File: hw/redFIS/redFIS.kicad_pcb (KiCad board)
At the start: 2 copper layers, 72 parts, among them J1 USB_B, J2 DE9_Plug, J3 Conn_01x04, J4 Conn_01x03, Q1 BC850, Q2 BC850, Q3 BC850, Q4 BC857, U1 ESP-32S, U2 AP63203WU, U3 AP63205WU, U4 TJA1049T, U5 CH340G, U6 PCM5102A, U7 AP63203WU, Y1 12Mhz

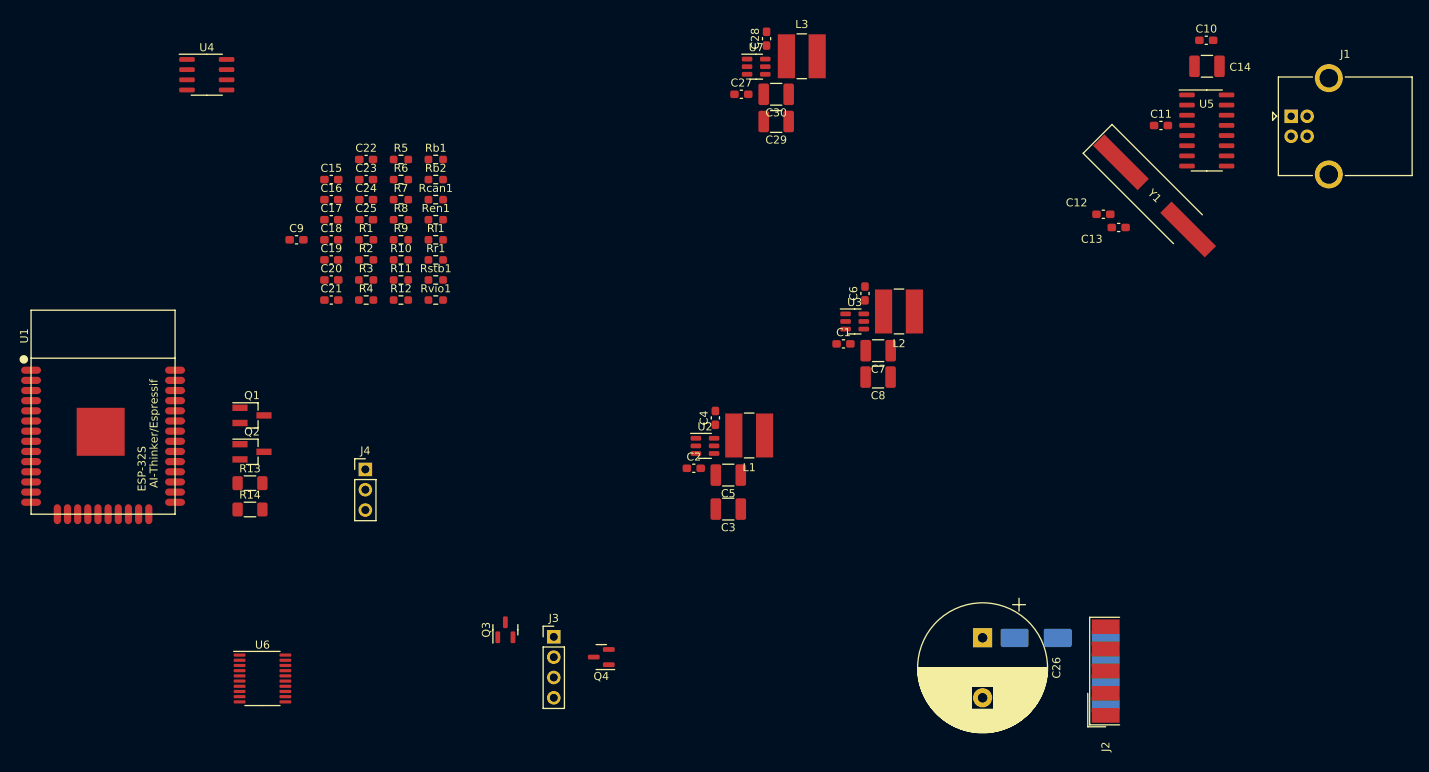
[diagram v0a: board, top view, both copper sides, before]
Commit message: Finished first version of PCB
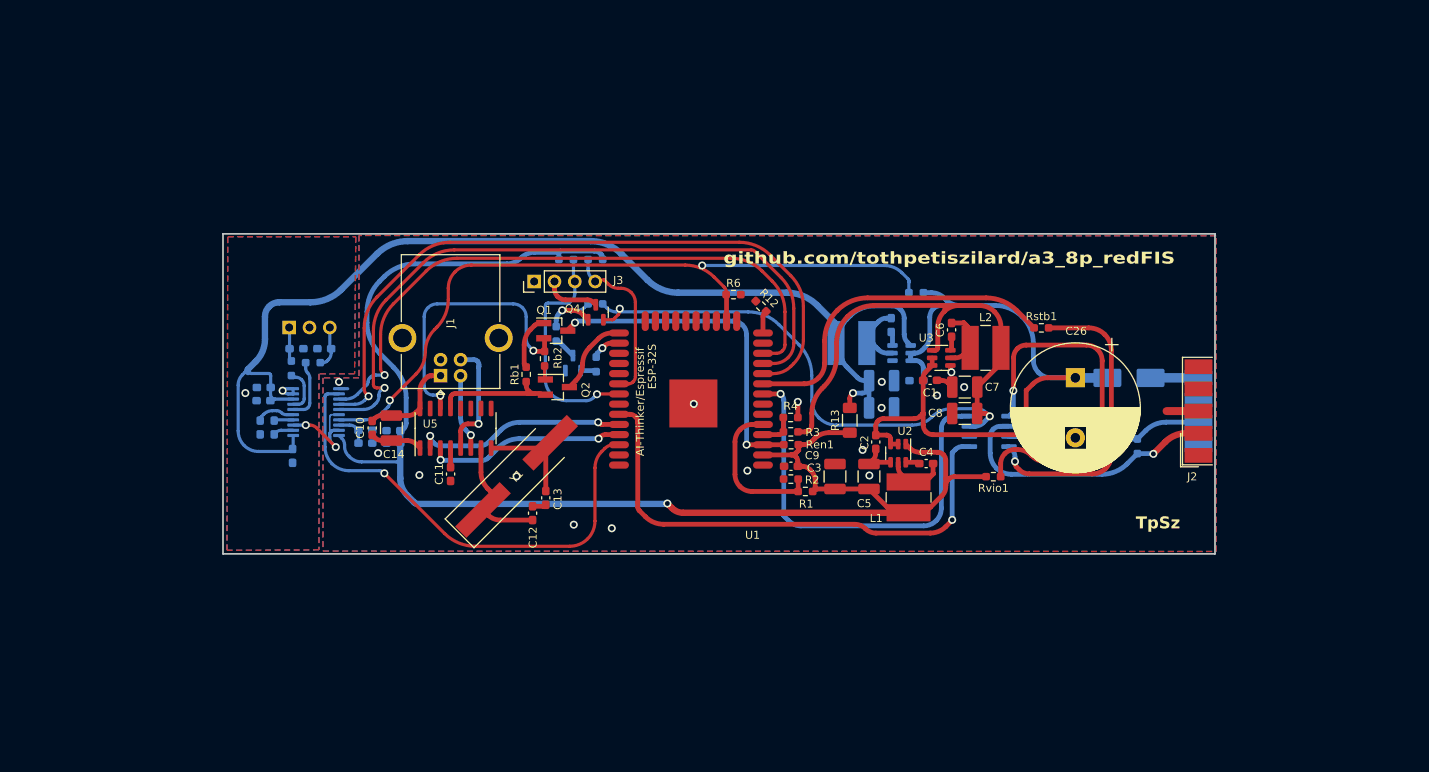
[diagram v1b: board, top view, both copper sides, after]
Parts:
- removed R14: 1R, Resistor_SMD:R_1206_3216Metric_Pad1.30x1.75mm_HandSolder
- C15, C16, C17, C18, C19, C20, C21, C22, C23, C24, C25, C27, C28, C29, C30, J4, L3, Q3, R10, R11, R5, R7, R8, R9, Rcan1, Rl1, Rr1, U4, U6, U7: moved to B.Cu
- moved C10 115.0 mm to (68.7, 74.2), turned to 90 degrees
- moved C14 111.5 mm to (71.0, 74.3), turned to -90 degrees
- moved J1 111.2 mm to (77.2, 67.7), turned to 90 degrees
- moved U4 107.5 mm to (145.8, 74.7)
- moved U5 101.0 mm to (79.1, 74.3), turned to 90 degrees
- moved C11 98.9 mm to (78.5, 80.0), turned to 90 degrees
- moved Rcan1 93.0 mm to (164.3, 76.5), turned to 90 degrees
- moved Y1 87.1 mm to (86.7, 80.3), turned to 45 degrees
- moved C12 80.5 mm to (88.7, 84.9), turned to -90 degrees
- moved C13 79.2 mm to (90.3, 83.0), turned to 90 degrees
- moved Rstb1 75.9 mm to (152.3, 61.8)
- moved R13 75.4 mm to (128.3, 73.3), turned to 90 degrees
- moved U1 73.7 mm to (108.4, 69.4), turned to 180 degrees
- moved Rvio1 73.1 mm to (146.3, 80.3), turned to 180 degrees
- moved C9 68.0 mm to (121.0, 79.0), turned to 180 degrees
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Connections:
- U1 pad 16: unconnected-(U1-IO13-Pad16) -> MUTE
- U1 pad 7: MUTE -> unconnected-(U1-IO35-Pad7)
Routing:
- net +3V3: track 0.00 -> 190.1 mm, vias 0 -> 1
- net +3.3VA: track 0.00 -> 147.2 mm, vias 0 -> 1
- net +5V: track 0.00 -> 124.6 mm, vias 0 -> 2
- net MUTE: track 0.00 -> 93.3 mm, vias 0 -> 2
- net +12V: track 0.00 -> 90.8 mm
- net I2S_DOUT: track 0.00 -> 88.7 mm, vias 0 -> 1
- net I2S_LRC: track 0.00 -> 86.8 mm, vias 0 -> 1
- net I2S_BCLK: track 0.00 -> 78.6 mm, vias 0 -> 1
- net CANTXD: track 0.00 -> 65.3 mm, vias 0 -> 1
- net I2S_SCK: track 0.00 -> 60.4 mm, vias 0 -> 1
- net CANRXD: track 0.00 -> 53.3 mm, vias 0 -> 1
- net Net-(U4-SPLIT): track 0.00 -> 48.2 mm, vias 0 -> 1
- net STB: track 0.00 -> 42.4 mm
- net ESP_EN: track 0.00 -> 42.1 mm, vias 0 -> 2
- net GND: track 0.00 -> 39.7 mm, vias 0 -> 20
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- added copper zone on B.Cu, net GND
- added copper zone on F.Cu, net GND
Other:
- board outline added: 124 x 40 mm
- board text added: "Audi A3 8P Red FIS Project v1.0"
- board text added: "L G R"
- board text added: "TpSz"
- board text added: "github.com/tothpetiszilard/a3_8p_redFIS"

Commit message: HW design bugfix
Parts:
- added Q5: BC850, Package_TO_SOT_SMD:SOT-23, B.Cu at (156.6, 85.1)
- added Q6: BC857, Package_TO_SOT_SMD:SOT-23, B.Cu at (143.7, 82.5)
- added R14: 10k, Resistor_SMD:R_0603_1608Metric_Pad0.98x0.95mm_HandSolder, B.Cu at (131.4, 85.5)
- added R15: 5k, Resistor_SMD:R_0603_1608Metric_Pad0.98x0.95mm_HandSolder, B.Cu at (135.2, 86.5)
- added R16: 10k, Resistor_SMD:R_0603_1608Metric_Pad0.98x0.95mm_HandSolder, B.Cu at (149.3, 84.8)
- added R17: 10k, Resistor_SMD:R_0603_1608Metric_Pad0.98x0.95mm_HandSolder, B.Cu at (143.7, 85.7)
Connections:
- U4 pad 1: CANTXD -> Net-(Q6-C)
- U4 pad 4: CANRXD -> Net-(U4-RXD)
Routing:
- net CANRXD: track 53.3 -> 32.2 mm
- net Net-(U4-RXD): track 0.00 -> 19.3 mm

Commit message: Finished bugfixing of HW design v1
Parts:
- moved Q5 10.1 mm to (146.8, 82.6), turned to 0 degrees
- moved R16 7.34 mm to (142.3, 82.6)
- moved Q6 3.22 mm to (142.4, 79.5)
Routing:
- net +5V: track 124.6 -> 136.7 mm
- net CANTXD: track 65.3 -> 56.1 mm
- net Net-(Q5-C): track 0.00 -> 6.69 mm
- net Net-(Q6-C): track 0.00 -> 3.27 mm
- net Net-(Q5-B): track 0.00 -> 3.00 mm
- net Net-(U4-RXD): track 19.3 -> 18.4 mm
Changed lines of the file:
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@@
 	(footprint "Package_TO_SOT_SMD:SOT-23"
 		(layer "B.Cu")
-		(at 156.6 85.0625 90)
+		(at 146.8 82.6)
 		(descr "SOT, 3 Pin (https://www.jedec.org/system/files/docs/to-236h.pdf variant AB), generated with kicad-footprint-generator ipc_gullwing_generator.py")
 		(tags "SOT TO_SOT_SMD")
 		(property "Reference" "Q5"
-			(at 0 2.4 90)
+			(at 0 2.4 360)
 			(layer "B.SilkS")
 			(effects
@@
 		)
 		(property "Value" "BC850"
-			(at 0 -2.4 90)
+			(at 0 -2.4 360)
 			(layer "B.Fab")
 			(effects
@@
 		)
 		(property "Footprint" "Package_TO_SOT_SMD:SOT-23"
-			(at 0 0 90)
+			(at 0 0 360)
 			(layer "B.Fab")
 			(hide yes)
@@
 		)
 		(property "Datasheet" "http://www.infineon.com/dgdl/Infineon-BC847SERIES_BC848SERIES_BC849SERIES_BC850SERIES-DS-v01_01-en.pdf?fileId=db3a304314dca389011541d4630a1657"
-			(at 0 0 90)
+			(at 0 0 360)
 			(layer "B.Fab")
 			(hide yes)
@@
 		)
 		(property "Description" "0.1A Ic, 45V Vce, NPN Transistor, SOT-23"
-			(at 0 0 90)
+			(at 0 0 360)
 			(layer "B.Fab")
 			(hide yes)
@@
 		(attr smd)
 		(fp_line
-			(start 0.65 -1.56)
-			(end 0 -1.56)
+			(start -1.675 1.56)
+			(end 0 1.56)
 			(stroke
 				(width 0.12)
@@
 		)
 		(fp_line
-			(start 0.65 1.56)
-			(end 0 1.56)
+			(start 0.65 -1.56)
+			(end 0 -1.56)
 			(stroke
 				(width 0.12)
@@
 		)
 		(fp_line
-			(start -1.675 1.56)
+			(start 0.65 1.56)
 			(end 0 1.56)
 			(stroke
@@
 		)
 		(fp_line
-			(start 1.92 -1.7)
-			(end -1.92 -1.7)
+			(start -1.92 -1.7)
+			(end -1.92 1.7)
 			(stroke
 				(width 0.05)
@@
 		)
 		(fp_line
-			(start -1.92 -1.7)
-			(end -1.92 1.7)
+			(start -1.92 1.7)
+			(end 1.92 1.7)
 			(stroke
 				(width 0.05)
@@
 		)
 		(fp_line
-			(start 1.92 1.7)
-			(end 1.92 -1.7)
+			(start 1.92 -1.7)
+			(end -1.92 -1.7)
 			(stroke
 				(width 0.05)
@@
 		)
 		(fp_line
-			(start -1.92 1.7)
-			(end 1.92 1.7)
+			(start 1.92 1.7)
+			(end 1.92 -1.7)
 			(stroke
 				(width 0.05)
@@
 		)
 		(fp_line
-			(start 0.65 -1.45)
-			(end 0.65 1.45)
+			(start -0.65 -1.45)
+			(end 0.65 -1.45)
 			(stroke
 				(width 0.1)
@@
 		)
 		(fp_line
-			(start -0.65 -1.45)
-			(end 0.65 -1.45)
+			(start -0.65 1.125)
+			(end -0.65 -1.45)
 			(stroke
 				(width 0.1)
@@
 		)
 		(fp_line
-			(start -0.65 1.125)
-			(end -0.65 -1.45)
+			(start -0.325 1.45)
+			(end -0.65 1.125)
 			(stroke
 				(width 0.1)
@@
 		)
 		(fp_line
-			(start 0.65 1.45)
-			(end -0.325 1.45)
+			(start 0.65 -1.45)
+			(end 0.65 1.45)
 			(stroke
 				(width 0.1)
@@
 		)
 		(fp_line
-			(start -0.325 1.45)
-			(end -0.65 1.125)
+			(start 0.65 1.45)
+			(end -0.325 1.45)
 			(stroke
 				(width 0.1)
@@
 		)
 		(fp_text user "${REFERENCE}"
-			(at 0 0 90)
+			(at 0 0 360)
 			(layer "B.Fab")
 			(effects
@@
 		)
 		(pad "1" smd roundrect
-			(at -0.9375 0.95 90)
+			(at -0.9375 0.95)
 			(size 1.475 0.6)
 			(layers "B.Cu" "B.Paste" "B.Mask")
@@
 		)
 		(pad "2" smd roundrect
-			(at -0.9375 -0.95 90)
+			(at -0.9375 -0.95)
 			(size 1.475 0.6)
 			(layers "B.Cu" "B.Paste" "B.Mask")
@@
 		)
 		(pad "3" smd roundrect
-			(at 0.9375 0 90)
+			(at 0.9375 0)
 			(size 1.475 0.6)
 			(layers "B.Cu" "B.Paste" "B.Mask")
@@
 	(footprint "Package_TO_SOT_SMD:SOT-23"
 		(layer "B.Cu")
-		(at 143.7 82.4875 90)
+		(at 142.4 79.5375 90)
 		(descr "SOT, 3 Pin (https://www.jedec.org/system/files/docs/to-236h.pdf variant AB), generated with kicad-footprint-generator ipc_gullwing_generator.py")
 		(tags "SOT TO_SOT_SMD")
@@
 	(footprint "Resistor_SMD:R_0603_1608Metric_Pad0.98x0.95mm_HandSolder"
 		(layer "B.Cu")
-		(at 149.3125 84.8)
+		(at 142.3125 82.6)
 		(descr "Resistor SMD 0603 (1608 Metric), square (rectangular) end terminal, IPC_7351 nominal with elongated pad for handsoldering. (Body size source: IPC-SM-782 page 72, https://www.pcb-3d.com/wordpress/wp-content/uploads/ipc-sm-782a_amendment_1_and_2.pdf), generated with kicad-footprint-generator")
 		(tags "resistor handsolder")
@@
 	)
 	(segment
+		(start 140.4 80.2)
+		(end 140.675 80.475)
+		(width 0.4)
+		(layer "B.Cu")
+		(net 8)
+	)
+	(segment
+		(start 140.4 74.4)
+		(end 140.4 80.2)
+		(width 0.4)
+		(layer "B.Cu")
+		(net 8)
+	)
+	(segment
 		(start 119.493792 61.343792)
 		(end 122.006207 63.856207)
@@
 	)
 	(segment
+		(start 140.75 74.05)
+		(end 140.4 74.4)
+		(width 0.4)
+		(layer "B.Cu")
+		(net 8)
+	)
+	(segment
+		(start 141.4 82.6)
+		(end 141.4 80.525)
+		(width 0.4)
+		(layer "B.Cu")
+		(net 8)
+	)
+	(segment
 		(start 145.85 72.8)
 		(end 145.375 72.325)
@@
 	)
 	(segment
+		(start 140.675 80.475)
+		(end 141.45 80.475)
+		(width 0.4)
+		(layer "B.Cu")
+		(net 8)
+	)
+	(segment
 		(start 97.9625 59.25)
 		(end 97.4625 58.75)
@@
 	)
 	(segment
+		(start 141.4 80.525)
+		(end 141.45 80.475)
+		(width 0.4)
+		(layer "B.Cu")
+		(net 8)
+	)
+	(segment
+		(start 143.3 74.05)
+		(end 140.75 74.05)
+		(width 0.4)
+		(layer "B.Cu")
+		(net 8)
+	)
+	(segment
 		(start 143.95 74.05)
 		(end 143.3 74.05)
@@
 	)
 	(segment
-		(start 141.15 85.75)
-		(end 141.15 77.385355)
-		(width 0.6)
-		(layer "B.Cu")
-		(net 60)
-	)
-	(segment
-		(start 141.225 77.275)
-		(end 141.175 77.325)
-		(width 0.6)
-		(layer "B.Cu")
-		(net 60)
-	)
-	(segment
-		(start 141.225 77.275)
-		(end 141.555 76.945)
-		(width 0.6)
-		(layer "B.Cu")
-		(net 60)
-	)
-	(segment
-		(start 142.412045 76.59)
-		(end 143.3 76.59)
+		(start 142.6875 85.75)
+		(end 142.7375 85.7)
 		(width 0.6)
 		(layer "B.Cu")
@@
 		(net 60)
 	)
-	(arc
-		(start 142.412045 76.59)
-		(mid 141.948215 76.682261)
-		(end 141.555 76.945)
-		(width 0.6)
-		(layer "B.Cu")
-		(net 60)
-	)
-	(arc
-		(start 141.175 77.325)
-		(mid 141.156497 77.352691)
-		(end 141.15 77.385355)
+	(segment
+		(start 141.15 85.75)
+		(end 142.6875 85.75)
 		(width 0.6)
 		(layer "B.Cu")
@@
 	)
 	(segment
-		(start 142.290858 72.8)
-		(end 141.336396 72.8)
-		(width 0.6)
+		(start 145.1 85.7)
+		(end 145.8625 84.9375)
+		(width 0.4)
 		(layer "B.Cu")
-		(net 85)
+		(net 82)
 	)
 	(segment
-		(start 137.580761 86.5)
-		(end 136.0625 86.5)
-		(width 0.6)
+		(start 145.8625 84.9375)
+		(end 145.8625 83.55)
+		(width 0.4)
 		(layer "B.Cu")
-		(net 85)
+		(net 82)
+	)
+	(segment
+		(start 144.5625 85.7)
+		(end 145.1 85.7)
+		(width 0.4)
+		(layer "B.Cu")
+		(net 82)
+	)
+	(segment
+		(start 143.225 80.6)
+		(end 143.35 80.475)
+		(width 0.4)
+		(layer "B.Cu")
+		(net 83)
+	)
+	(segment
+		(start 143.225 82.6)
+		(end 147.7375 82.6)
+		(width 0.4)
+		(layer "B.Cu")
+		(net 83)
 	)
 	(segment
-		(start 139.8 74.336396)
-		(end 139.8 84.280761)
+		(start 143.225 82.6)
+		(end 143.225 80.6)
+		(width 0.4)
+		(layer "B.Cu")
+		(net 83)
+	)
+	(segment
+		(start 142.412045 76.59)
+		(end 143.3 76.59)
 		(width 0.6)
 		(layer "B.Cu")
-		(net 85)
+		(net 84)
 	)
 	(segment
-		(start 142.339143 72.78)
-		(end 143.3 72.78)
+		(start 142.4 78.6)
+		(end 142.4 77.49)
+		(width 0.4)
+		(layer "B.Cu")
+		(net 84)
+	)
+	(segment
+		(start 142.4 77.49)
+		(end 143.3 76.59)
+		(width 0.4)
+		(layer "B.Cu")
+		(net 84)
+	)
+	(segment
+		(start 143.3 72.78)
+		(end 142.339143 72.78)
 		(width 0.6)
 		(layer "B.Cu")
 		(net 85)
 	)
-	(arc
-		(start 140.25 73.25)
-		(mid 139.916951 73.748442)
-		(end 139.8 74.336396)
+	(segment
+		(start 139 83.5625)
+		(end 136.0625 86.5)
 		(width 0.6)
 		(layer "B.Cu")
 		(net 85)
 	)
-	(arc
-		(start 142.315001 72.79)
-		(mid 142.303924 72.797401)
-		(end 142.290858 72.8)
+	(segment
+		(start 139 74.2)
+		(end 139 83.5625)
 		(width 0.6)
 		(layer "B.Cu")
 		(net 85)
 	)
-	(arc
-		(start 142.339143 72.78)
-		(mid 142.326077 72.782598)
-		(end 142.315001 72.79)
+	(segment
+		(start 142.290858 72.8)
+		(end 140.4 72.8)
 		(width 0.6)
 		(layer "B.Cu")
 		(net 85)
 	)
-	(arc
-		(start 139.15 85.85)
-		(mid 138.430027 86.33107)
-		(end 137.580761 86.5)
+	(segment
+		(start 140.4 72.8)
+		(end 139 74.2)
 		(width 0.6)
 		(layer "B.Cu")
@@
 	)
 	(arc
-		(start 141.336396 72.8)
-		(mid 140.748442 72.916951)
-		(end 140.25 73.25)
+		(start 142.339143 72.78)
+		(mid 142.326077 72.782598)
+		(end 142.315001 72.79)
 		(width 0.6)
 		(layer "B.Cu")
@@
 	)
 	(arc
-		(start 139.8 84.280761)
-		(mid 139.63107 85.130027)
-		(end 139.15 85.85)
+		(start 142.315001 72.79)
+		(mid 142.303924 72.797401)
+		(end 142.290858 72.8)
 		(width 0.6)
 		(layer "B.Cu")

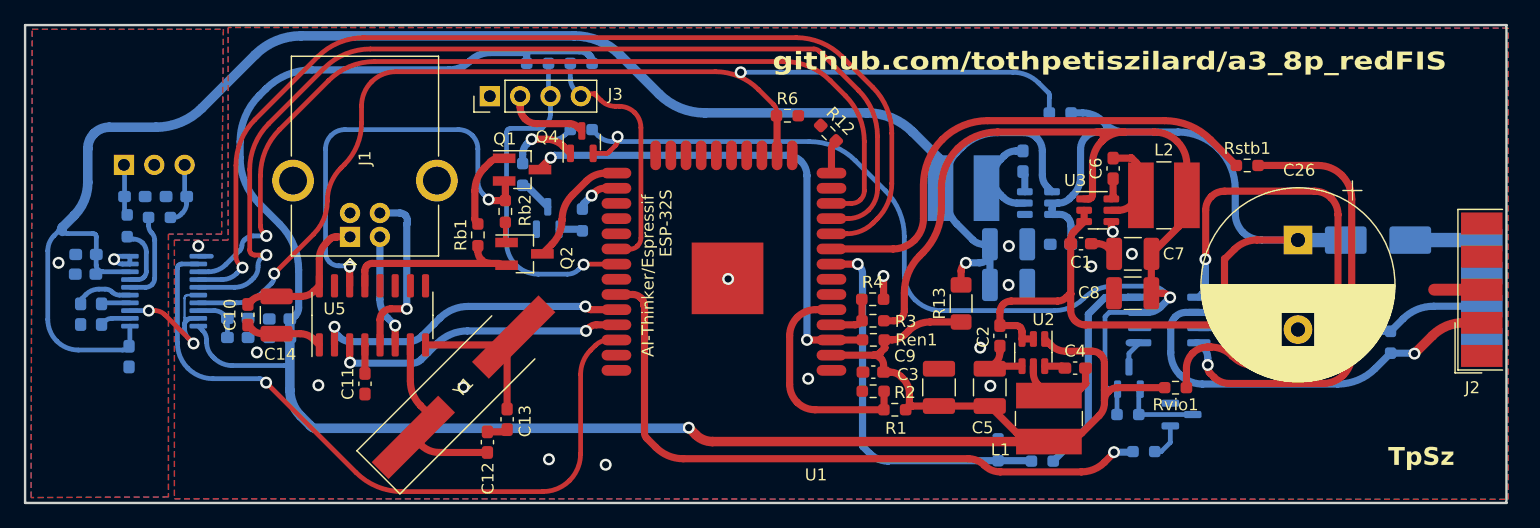
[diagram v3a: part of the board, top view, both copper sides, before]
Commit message: PCB update - Almost forget to round the tracks...
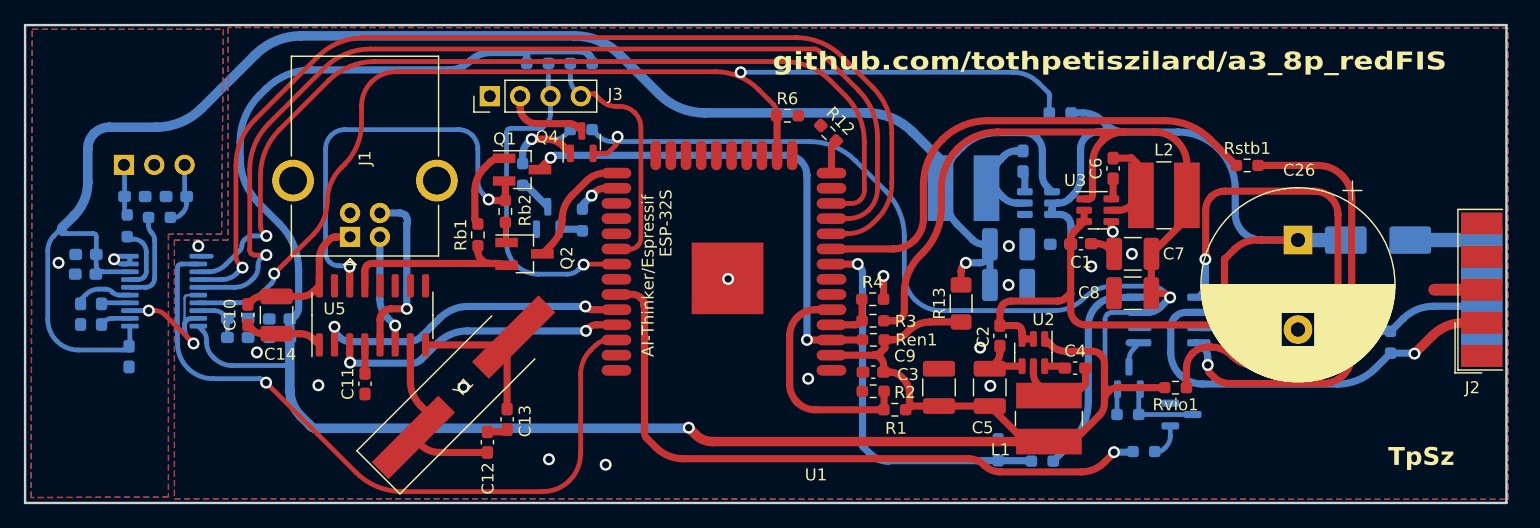
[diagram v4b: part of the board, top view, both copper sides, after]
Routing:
- net Net-(Q6-C): track 3.27 -> 2.73 mm
